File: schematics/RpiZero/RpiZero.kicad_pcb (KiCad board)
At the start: 2 copper layers, 1 part, among them U1 8_cells_battery

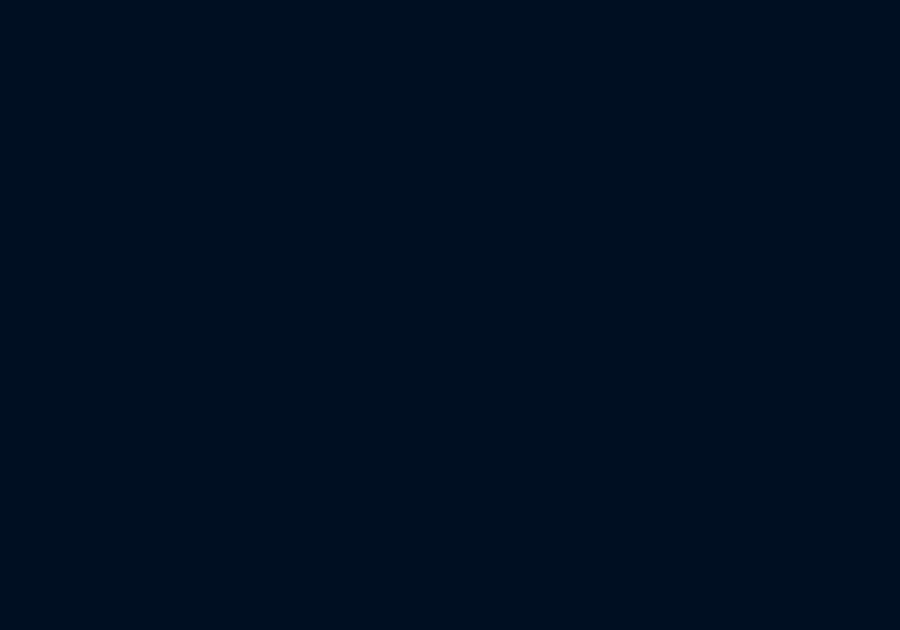
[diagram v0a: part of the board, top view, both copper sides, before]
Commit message: Update: added ADC MUX, voltage reference and battery pack symbol
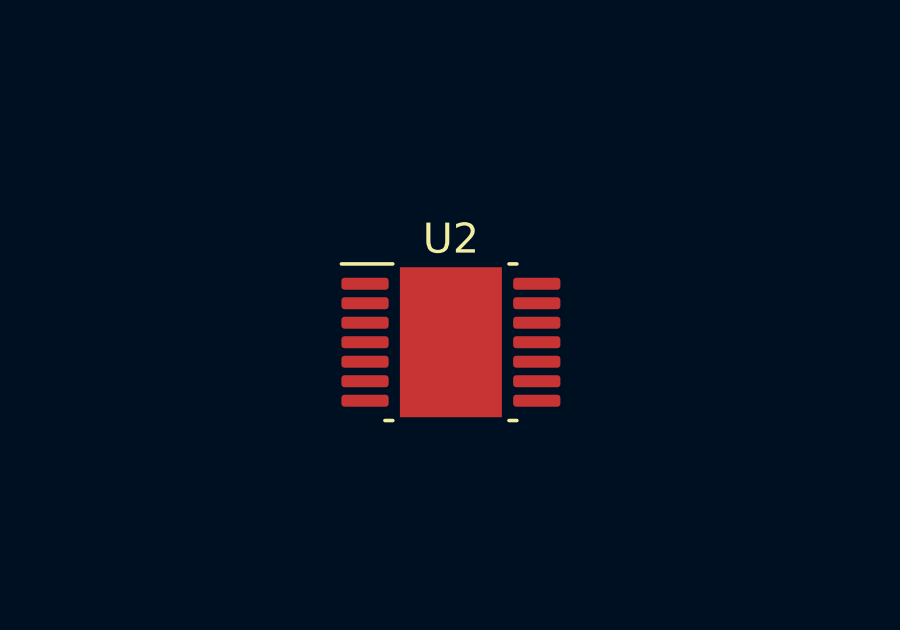
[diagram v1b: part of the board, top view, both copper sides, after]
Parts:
- added U2: LMV324, Package_SO:HTSSOP-14-1EP_4.4x5mm_P0.65mm_EP3.4x5mm_Mask3x3.1mm, F.Cu at (157.7, 90.2)
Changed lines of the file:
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@@
   (net 15 "unconnected-(U1-Pad15)")
   (net 16 "unconnected-(U1-Pad16)")
+  (net 17 "unconnected-(U2-Pad1)")
+  (net 18 "unconnected-(U2-Pad2)")
+  (net 19 "unconnected-(U2-Pad3)")
+  (net 20 "unconnected-(U2-Pad4)")
+  (net 21 "unconnected-(U2-Pad5)")
+  (net 22 "unconnected-(U2-Pad6)")
+  (net 23 "unconnected-(U2-Pad7)")
+  (net 24 "Net-(U2-Pad8)")
+  (net 25 "unconnected-(U2-Pad9)")
+  (net 26 "unconnected-(U2-Pad11)")
+  (net 27 "Net-(U2-Pad12)")
+  (net 28 "unconnected-(U2-Pad13)")
+  (footprint "Package_SO:HTSSOP-14-1EP_4.4x5mm_P0.65mm_EP3.4x5mm_Mask3x3.1mm" (layer "F.Cu")
+    (at 157.734 90.17)
+    (descr "HTSSOP, 14 Pin (http://www.ti.com/lit/ds/symlink/lm5161.pdf#page=34), generated with kicad-footprint-generator ipc_gullwing_generator.py")
+    (tags "HTSSOP SO")
+    (property "Sheetfile" "RpiZero.kicad_sch")
+    (property "Sheetname" "")
+    (attr smd)
+    (fp_text reference "U2" (at 0 -3.45) (layer "F.SilkS")
+      (effects (font (size 1 1) (thickness 0.15)))
+    )
+    (fp_text value "LMV324" (at 0 3.45) (layer "F.Fab")
+      (effects (font (size 1 1) (thickness 0.15)))
+    )
+    (fp_text user "${REFERENCE}" (at 0 0) (layer "F.Fab")
+      (effects (font (size 1 1) (thickness 0.15)))
+    )
+    (fp_line (start 1.935584 2.61) (end 2.2 2.61) (layer "F.SilkS") (width 0.12))
+    (fp_line (start -1.935584 2.61) (end -2.2 2.61) (layer "F.SilkS") (width 0.12))
+    (fp_line (start 1.935584 -2.61) (end 2.2 -2.61) (layer "F.SilkS") (width 0.12))
+    (fp_line (start -1.935584 -2.61) (end -3.65 -2.61) (layer "F.SilkS") (width 0.12))
+    (fp_line (start 3.9 -2.75) (end -3.9 -2.75) (layer "F.CrtYd") (width 0.05))
+    (fp_line (start -3.9 -2.75) (end -3.9 2.75) (layer "F.CrtYd") (width 0.05))
+    (fp_line (start -3.9 2.75) (end 3.9 2.75) (layer "F.CrtYd") (width 0.05))
+    (fp_line (start 3.9 2.75) (end 3.9 -2.75) (layer "F.CrtYd") (width 0.05))
+    (fp_line (start -1.2 -2.5) (end 2.2 -2.5) (layer "F.Fab") (width 0.1))
+    (fp_line (start 2.2 2.5) (end -2.2 2.5) (layer "F.Fab") (width 0.1))
+    (fp_line (start 2.2 -2.5) (end 2.2 2.5) (layer "F.Fab") (width 0.1))
+    (fp_line (start -2.2 -1.5) (end -1.2 -2.5) (layer "F.Fab") (width 0.1))
+    (fp_line (start -2.2 2.5) (end -2.2 -1.5) (layer "F.Fab") (width 0.1))
+    (pad "" smd rect (at 0 0) (size 3 3.1) (layers "F.Mask"))
+    (pad "" smd roundrect (at 0.75 -0.775) (size 1.21 1.25) (layers "F.Paste") (roundrect_rratio 0.206612))
+    (pad "" smd roundrect (at -0.75 -0.775) (size 1.21 1.25) (layers "F.Paste") (roundrect_rratio 0.206612))
+    (pad "" smd roundrect (at 0.75 0.775) (size 1.21 1.25) (layers "F.Paste") (roundrect_rratio 0.206612))
+    (pad "" smd roundrect (at -0.75 0.775) (size 1.21 1.25) (layers "F.Paste") (roundrect_rratio 0.206612))
+    (pad "1" smd roundrect (at -2.8625 -1.95) (size 1.575 0.4) (layers "F.Cu" "F.Paste" "F.Mask") (roundrect_rratio 0.25)
+      (net 17 "unconnected-(U2-Pad1)") (pintype "output"))
+    (pad "2" smd roundrect (at -2.8625 -1.3) (size 1.575 0.4) (layers "F.Cu" "F.Paste" "F.Mask") (roundrect_rratio 0.25)
+      (net 18 "unconnected-(U2-Pad2)") (pinfunction "-") (pintype "input"))
+    (pad "3" smd roundrect (at -2.8625 -0.65) (size 1.575 0.4) (layers "F.Cu" "F.Paste" "F.Mask") (roundrect_rratio 0.25)
+      (net 19 "unconnected-(U2-Pad3)") (pinfunction "+") (pintype "input"))
+    (pad "4" smd roundrect (at -2.8625 0) (size 1.575 0.4) (layers "F.Cu" "F.Paste" "F.Mask") (roundrect_rratio 0.25)
+      (net 20 "unconnected-(U2-Pad4)") (pinfunction "V+") (pintype "power_in"))
+    (pad "5" smd roundrect (at -2.8625 0.65) (size 1.575 0.4) (layers "F.Cu" "F.Paste" "F.Mask") (roundrect_rratio 0.25)
+      (net 21 "unconnected-(U2-Pad5)") (pinfunction "+") (pintype "input"))
+    (pad "6" smd roundrect (at -2.8625 1.3) (size 1.575 0.4) (layers "F.Cu" "F.Paste" "F.Mask") (roundrect_rratio 0.25)
+      (net 22 "unconnected-(U2-Pad6)") (pinfunction "-") (pintype "input"))
+    (pad "7" smd roundrect (at -2.8625 1.95) (size 1.575 0.4) (layers "F.Cu" "F.Paste" "F.Mask") (roundrect_rratio 0.25)
+      (net 23 "unconnected-(U2-Pad7)") (pintype "output"))
+    (pad "8" smd roundrect (at 2.8625 1.95) (size 1.575 0.4) (layers "F.Cu" "F.Paste" "F.Mask") (roundrect_rratio 0.25)
+      (net 24 "Net-(U2-Pad8)") (pintype "output"))
+    (pad "9" smd roundrect (at 2.8625 1.3) (size 1.575 0.4) (layers "F.Cu" "F.Paste" "F.Mask") (roundrect_rratio 0.25)
+      (net 25 "unconnected-(U2-Pad9)") (pinfunction "-") (pintype "input"))
+    (pad "10" smd roundrect (at 2.8625 0.65) (size 1.575 0.4) (layers "F.Cu" "F.Paste" "F.Mask") (roundrect_rratio 0.25)
+      (net 24 "Net-(U2-Pad8)") (pinfunction "+") (pintype "input"))
+    (pad "11" smd roundrect (at 2.8625 0) (size 1.575 0.4) (layers "F.Cu" "F.Paste" "F.Mask") (roundrect_rratio 0.25)
+      (net 26 "unconnected-(U2-Pad11)") (pinfunction "V-") (pintype "power_in"))
+    (pad "12" smd roundrect (at 2.8625 -0.65) (size 1.575 0.4) (layers "F.Cu" "F.Paste" "F.Mask") (roundrect_rratio 0.25)
+      (net 27 "Net-(U2-Pad12)") (pinfunction "+") (pintype "input"))
+    (pad "13" smd roundrect (at 2.8625 -1.3) (size 1.575 0.4) (layers "F.Cu" "F.Paste" "F.Mask") (roundrect_rratio 0.25)
+      (net 28 "unconnected-(U2-Pad13)") (pinfunction "-") (pintype "input"))
+    (pad "14" smd roundrect (at 2.8625 -1.95) (size 1.575 0.4) (layers "F.Cu" "F.Paste" "F.Mask") (roundrect_rratio 0.25)
+      (net 27 "Net-(U2-Pad12)") (pintype "output"))
+    (pad "15" smd rect (at 0 0) (size 3.4 5) (layers "F.Cu"))
+    (model "${KICAD6_3DMODEL_DIR}/Package_SO.3dshapes/HTSSOP-14-1EP_4.4x5mm_P0.65mm_EP3.4x5mm_Mask3x3.1mm.wrl"
+      (offset (xyz 0 0 0))
+      (scale (xyz 1 1 1))
+      (rotate (xyz 0 0 0))
+    )
+  )
   (footprint "RpiZero:8_battery_celss" (layer "F.Cu")
     (at 128.778 88.265)
